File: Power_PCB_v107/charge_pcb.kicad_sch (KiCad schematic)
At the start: 47 parts

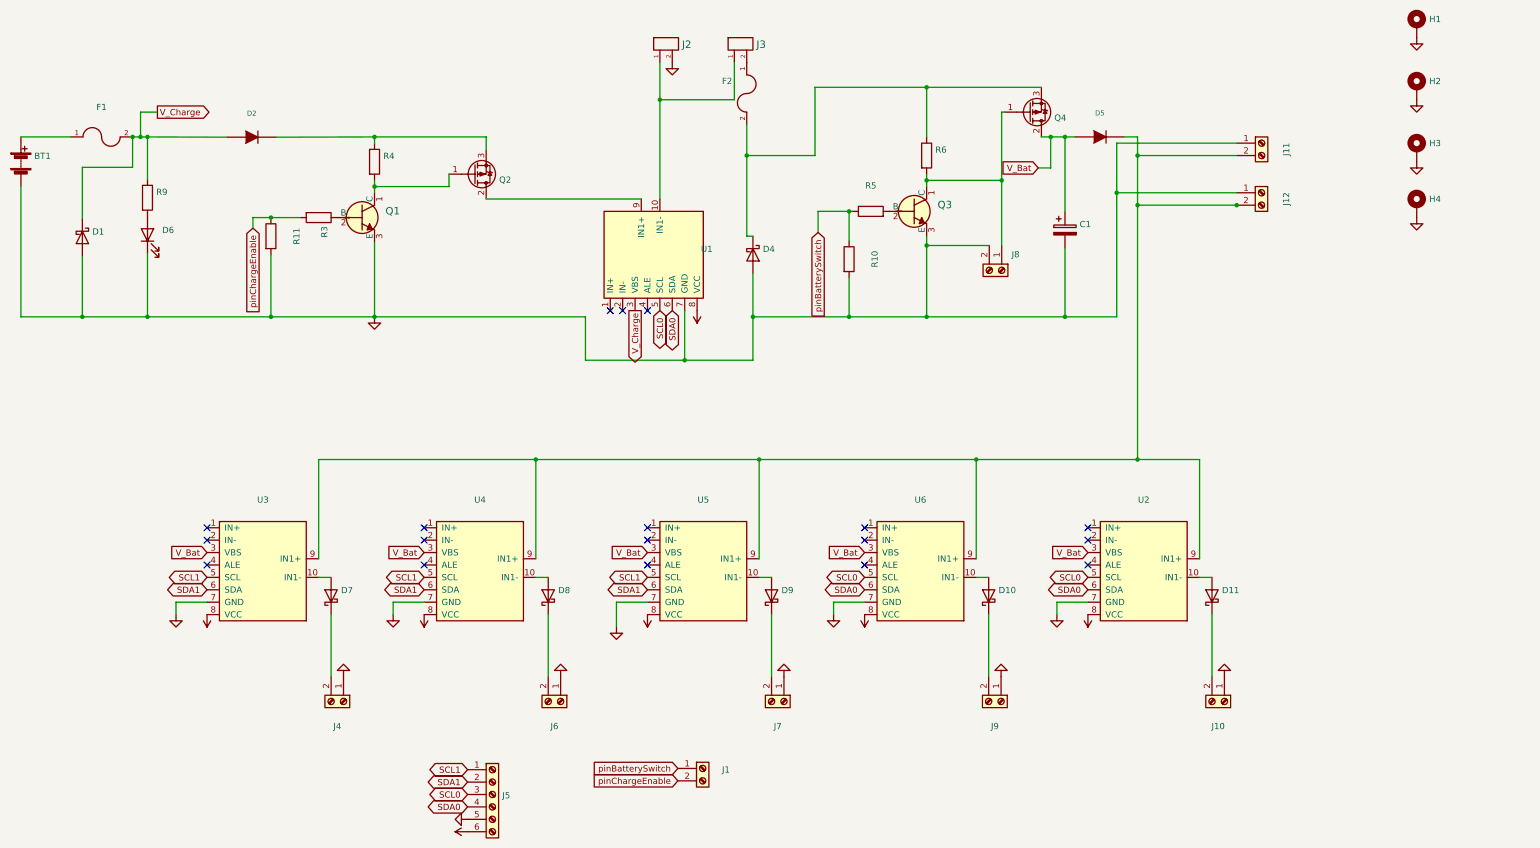
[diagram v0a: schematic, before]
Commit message: Rebuild Charge Board
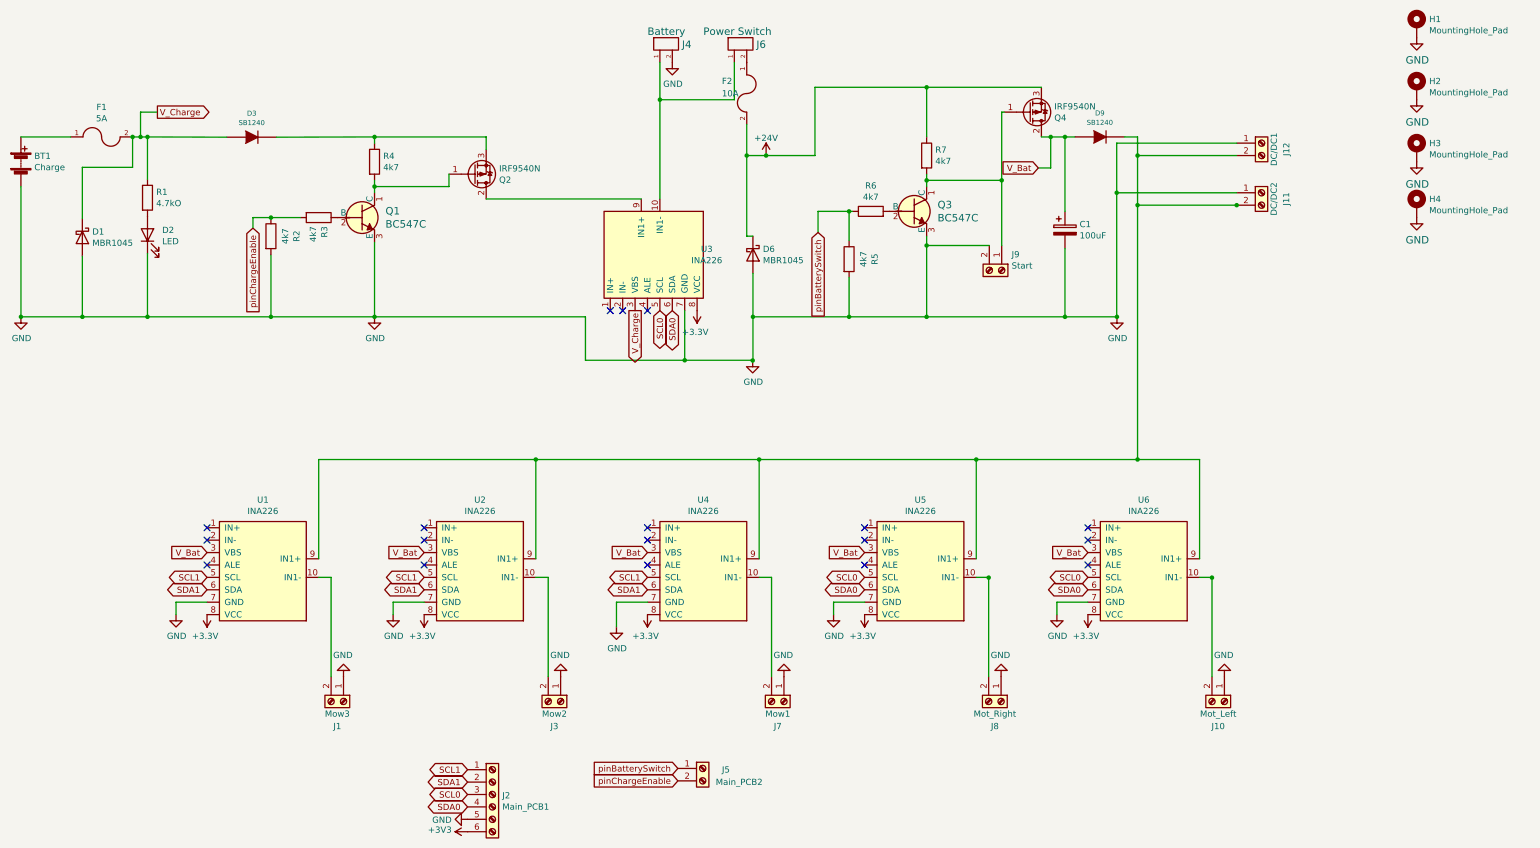
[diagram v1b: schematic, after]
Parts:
- removed D10, D11, D7, D8, D9: (no value), symbol Diode:MBR745
- BT1: value (none) -> Charge; footprint (none) -> Zimprich:Anschlussklemme_2P_RM5,08
- C1: value (none) -> 100uF; footprint (none) -> Zimprich:Elko_vert_11.2x6.3mm_RM2.5
- D1: value (none) -> MBR1045; footprint (none) -> Package_TO_SOT_THT:TO-220-2_Vertical
- D2: renamed from D6; value (none) -> LED; footprint (none) -> LED_THT:LED_D1.8mm_W3.3mm_H2.4mm
- D3: renamed from D2; value (none) -> SB1240; footprint (none) -> Diode_THT:D_DO-41_SOD81_P10.16mm_Horizontal
- D6: renamed from D4; value (none) -> MBR1045; footprint (none) -> Package_TO_SOT_THT:TO-220-2_Vertical
- D9: renamed from D5; value (none) -> SB1240; footprint (none) -> Diode_THT:D_DO-41_SOD81_P10.16mm_Horizontal
- F1: value (none) -> 5A; footprint (none) -> Zimprich:Fuseholder_Reichelt_PL112000
- F2: value (none) -> 10A; footprint (none) -> Zimprich:Fuseholder_Reichelt_PL112000
- H1, H2, H3, H4: value (none) -> MountingHole_Pad; footprint (none) -> MountingHole:MountingHole_3.2mm_M3_DIN965_Pad_TopBottom
- J1: renamed from J4; value (none) -> Mow3; footprint (none) -> TerminalBlock:TerminalBlock_bornier-2_P5.08mm
- J10: value (none) -> Mot_Left; footprint (none) -> TerminalBlock:TerminalBlock_bornier-2_P5.08mm
- J11: renamed from J12; value (none) -> DC/DC2; footprint (none) -> TerminalBlock:TerminalBlock_bornier-2_P5.08mm
- J12: renamed from J11; value (none) -> DC/DC1; footprint (none) -> TerminalBlock:TerminalBlock_bornier-2_P5.08mm
- J2: renamed from J5; value (none) -> Main_PCB1; footprint (none) -> Connector_JST:JST_XH_B6B-XH-A_1x06_P2.50mm_Vertical
- J3: renamed from J6; value (none) -> Mow2; footprint (none) -> TerminalBlock:TerminalBlock_bornier-2_P5.08mm
- J4: renamed from J2; value (none) -> Battery; footprint (none) -> TerminalBlock:TerminalBlock_bornier-2_P5.08mm
- J5: renamed from J1; value (none) -> Main_PCB2; footprint (none) -> Connector_JST:JST_XH_B2B-XH-A_1x02_P2.50mm_Vertical
- J6: renamed from J3; value (none) -> Power Switch; footprint (none) -> TerminalBlock:TerminalBlock_bornier-2_P5.08mm
- J7: value (none) -> Mow1; footprint (none) -> TerminalBlock:TerminalBlock_bornier-2_P5.08mm
- J8: renamed from J9; value (none) -> Mot_Right; footprint (none) -> TerminalBlock:TerminalBlock_bornier-2_P5.08mm
- J9: renamed from J8; value (none) -> Start; footprint (none) -> Connector_JST:JST_XH_B2B-XH-A_1x02_P2.50mm_Vertical
- Q1, Q3: value (none) -> BC547C; footprint (none) -> digikey-footprints:TO-92-3_Formed_Leads
- Q2, Q4: value (none) -> IRF9540N; footprint (none) -> Package_TO_SOT_THT:TO-220-3_Vertical
- R1: renamed from R9; value (none) -> 4.7kO; footprint (none) -> Resistor_THT:R_Axial_DIN0207_L6.3mm_D2.5mm_P7.62mm_Horizontal
- R2: renamed from R11; value (none) -> 4k7; footprint (none) -> Resistor_THT:R_Axial_DIN0207_L6.3mm_D2.5mm_P7.62mm_Horizontal
- R3, R4: value (none) -> 4k7; footprint (none) -> Resistor_THT:R_Axial_DIN0207_L6.3mm_D2.5mm_P7.62mm_Horizontal
- R5: renamed from R10; value (none) -> 4k7; footprint (none) -> Resistor_THT:R_Axial_DIN0207_L6.3mm_D2.5mm_P7.62mm_Horizontal
- R6: renamed from R5; value (none) -> 4k7; footprint (none) -> Resistor_THT:R_Axial_DIN0207_L6.3mm_D2.5mm_P7.62mm_Horizontal
- R7: renamed from R6; value (none) -> 4k7; footprint (none) -> Resistor_THT:R_Axial_DIN0207_L6.3mm_D2.5mm_P7.62mm_Horizontal
- U1: renamed from U3; value (none) -> INA226; footprint (none) -> Current_sense:INA226
- U2: renamed from U4; value (none) -> INA226; footprint (none) -> Current_sense:INA226
- U3: renamed from U1; value (none) -> INA226; footprint (none) -> Current_sense:INA226
- U4: renamed from U5; value (none) -> INA226; footprint (none) -> Current_sense:INA226
- U5: renamed from U6; value (none) -> INA226; footprint (none) -> Current_sense:INA226
- U6: renamed from U2; value (none) -> INA226; footprint (none) -> Current_sense:INA226
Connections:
- net +24V: now reaches D6.1 (K), F2.2, Q4.3 (S), R7.1
- net at U6.10 (IN1-): now also J10.2 (Pin_2)
- net at U5.10 (IN1-): now also J8.2 (Pin_2)
- net at U4.10 (IN1-): now also J7.2 (Pin_2)
- net at U2.10 (IN1-): now also J3.2 (Pin_2)
- net at U1.10 (IN1-): now also J1.2 (Pin_2)

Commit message: Don' know anymore
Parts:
- added JP1: Jumper_2_Open, Connector_PinHeader_2.54mm:PinHeader_1x02_P2.54mm_Vertical, symbol Jumper:Jumper_2_Open
- renumbered D3 to D2, D2 to D3, D6 to D4, D9 to D5
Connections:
- net V_Bat: now also J11.2 (Pin_2), J12.2 (Pin_2), U1.9 (IN1+), U2.9 (IN1+), U4.9 (IN1+), U5.9 (IN1+), U6.9 (IN1+), JP1.2 (B); no longer C1.1, D5.1 (A), Q4.2 (D)
- net at D2.2 (K), Q2.3 (S), R4.1: now also R1.1, JP1.1 (A)
- net at Q2.2 (D), U3.9 (IN1+): now also U3.3 (VBS)
- net +24V: no longer names the net of D4.1 (K), F2.2
- net +24V: now also D5.1 (A); no longer Q4.3 (S), R7.1
- net V_Charge: no longer names the net of D1.1 (K), D2.1 (A), F1.2
- net V_Charge: no longer R1.1, U3.3 (VBS)
- new net: D5.2 (K), Q4.3 (S), R7.1
- new net: C1.1, Q4.2 (D)
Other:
- moved on the sheet: D2, D3, D5, R1

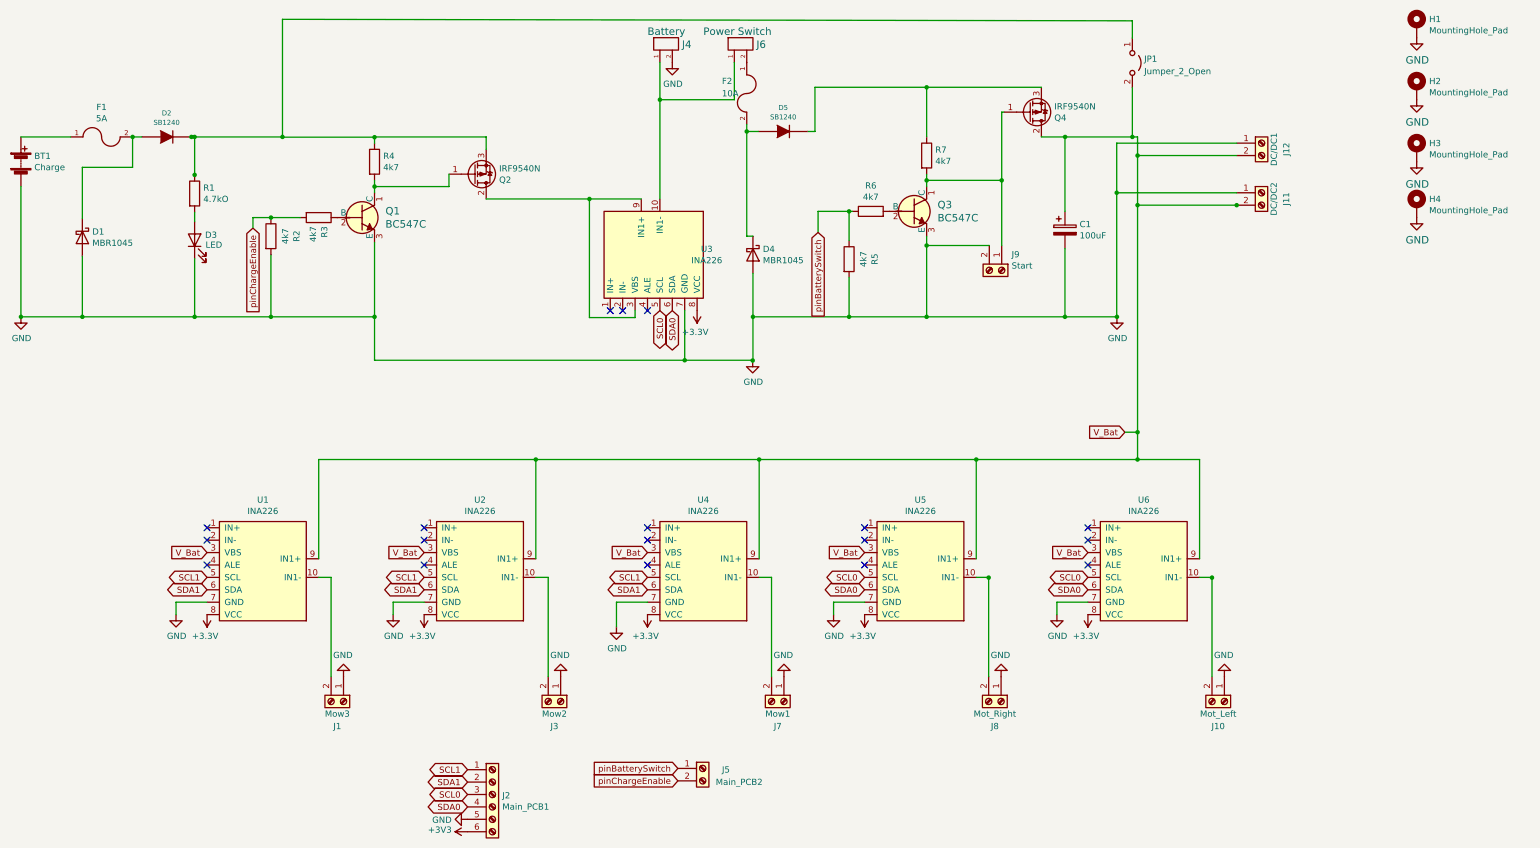
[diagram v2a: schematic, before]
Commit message: Add Labeling and PCB Routing
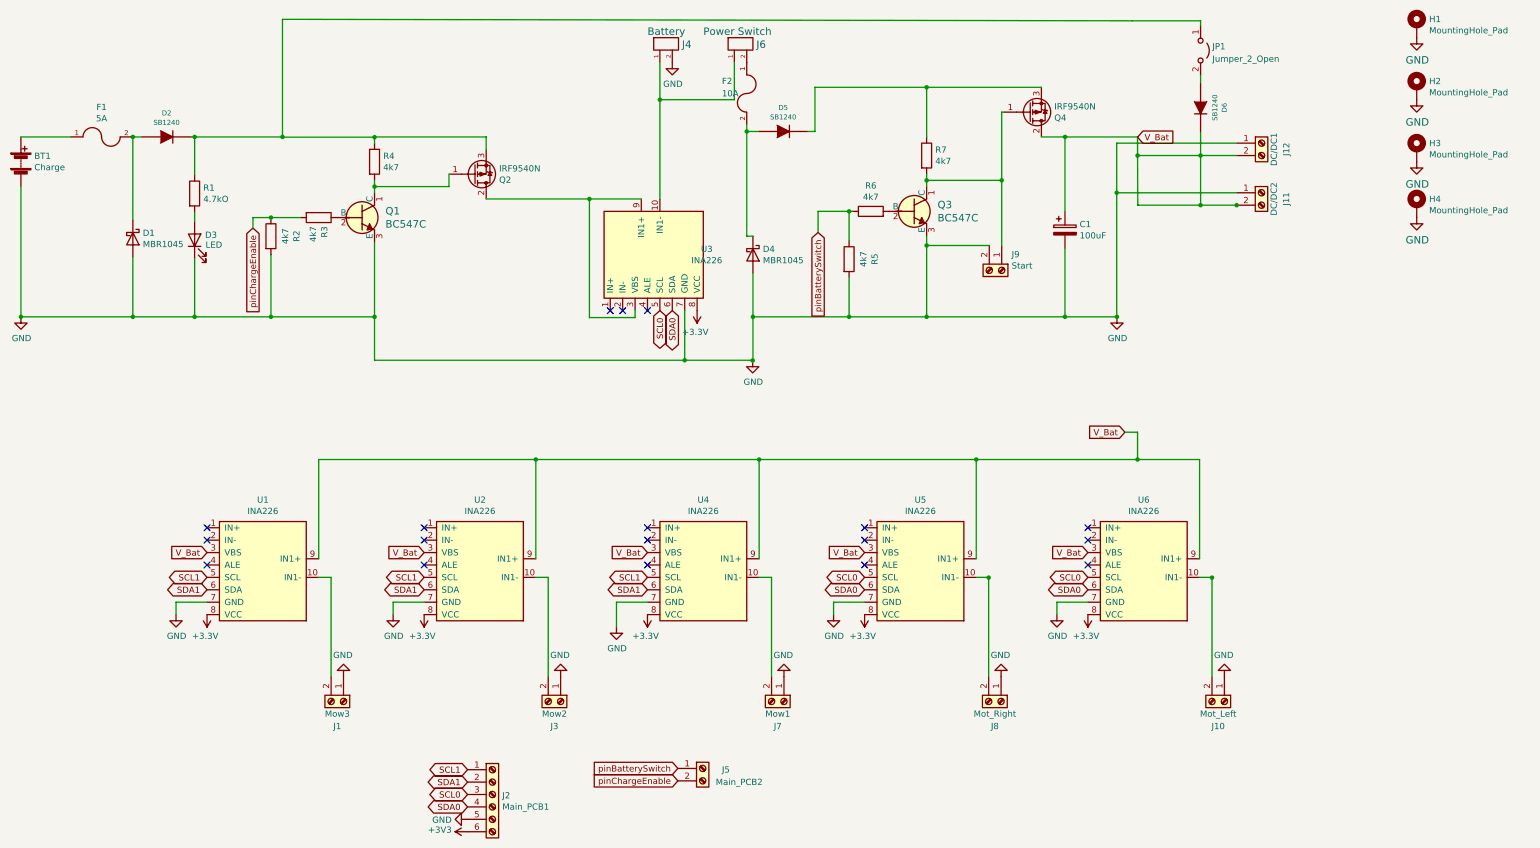
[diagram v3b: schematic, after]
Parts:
- added D6: SB1240, Diode_THT:D_DO-41_SOD81_P10.16mm_Horizontal, symbol charge_pcb-rescue:DIODE-Lötpad_2,5mm-charge_pcb-rescue
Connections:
- net V_Bat: now also D6.2 (K); no longer JP1.2 (B)
- new net: D6.1 (A), JP1.2 (B)
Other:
- title: (none) -> Charge PCB
- moved on the sheet: D1, JP1

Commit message: Wifi Sender Update Label
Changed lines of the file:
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@@
     (stroke (width 0) (type default) (color 0 0 0 0))
   )
-  (wire (pts (xy 229.0064 36.83) (xy 243.84 36.83))
+  (wire (pts (xy 229.0064 36.83) (xy 243.332 34.4424))
     (stroke (width 0) (type default) (color 0 0 0 0))
   )
@@
     (stroke (width 0) (type default) (color 0 0 0 0))
   )
-  (wire (pts (xy 243.84 36.83) (xy 243.84 40.64))
+  (wire (pts (xy 243.332 34.4424) (xy 243.84 40.64))
     (stroke (width 0) (type default) (color 0 0 0 0))
   )
@@
     )
   )
-  (global_label "V_Bat" (shape input) (at 243.84 36.8808 0) (fields_autoplaced)
+  (global_label "V_Bat" (shape input) (at 243.332 34.4424 0) (fields_autoplaced)
     (effects (font (size 1.27 1.27)) (justify left))
-    (property "Intersheet References" "${INTERSHEET_REFS}" (id 0) (at 467.36 80.0608 0)
+    (property "Intersheet References" "${INTERSHEET_REFS}" (id 0) (at 466.852 77.6224 0)
       (effects (font (size 1.27 1.27)) hide)
     )
